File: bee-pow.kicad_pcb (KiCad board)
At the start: 2 copper layers, 29 x 53.3 mm, 34 parts, among them J1 Conn_01x02_Male, J2 Conn_01x02_Male, J3 Conn_01x02_Male, J4 Conn_01x02_Male, J5 Screw_Terminal_01x04, U1 L7805, U2 L7815, U3 L7915

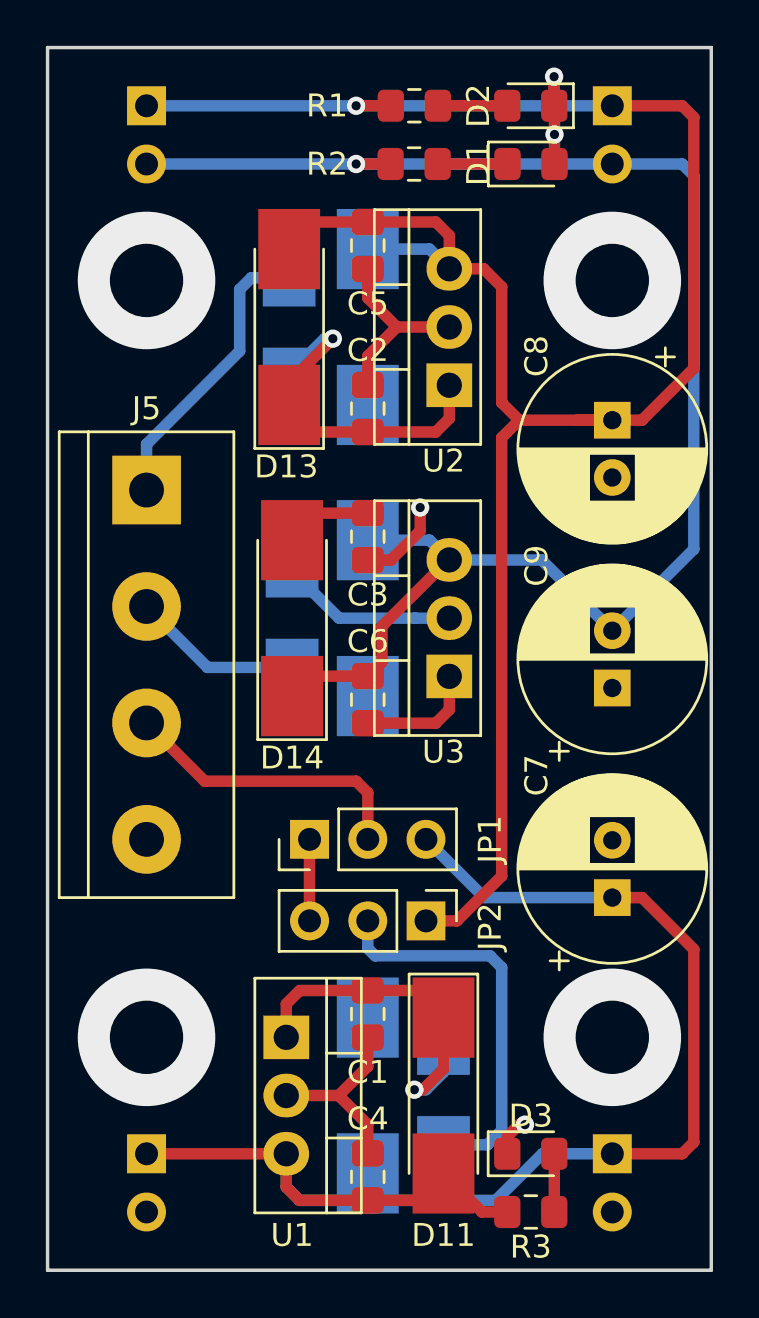
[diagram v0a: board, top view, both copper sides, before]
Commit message: Update labels and mounting holes.
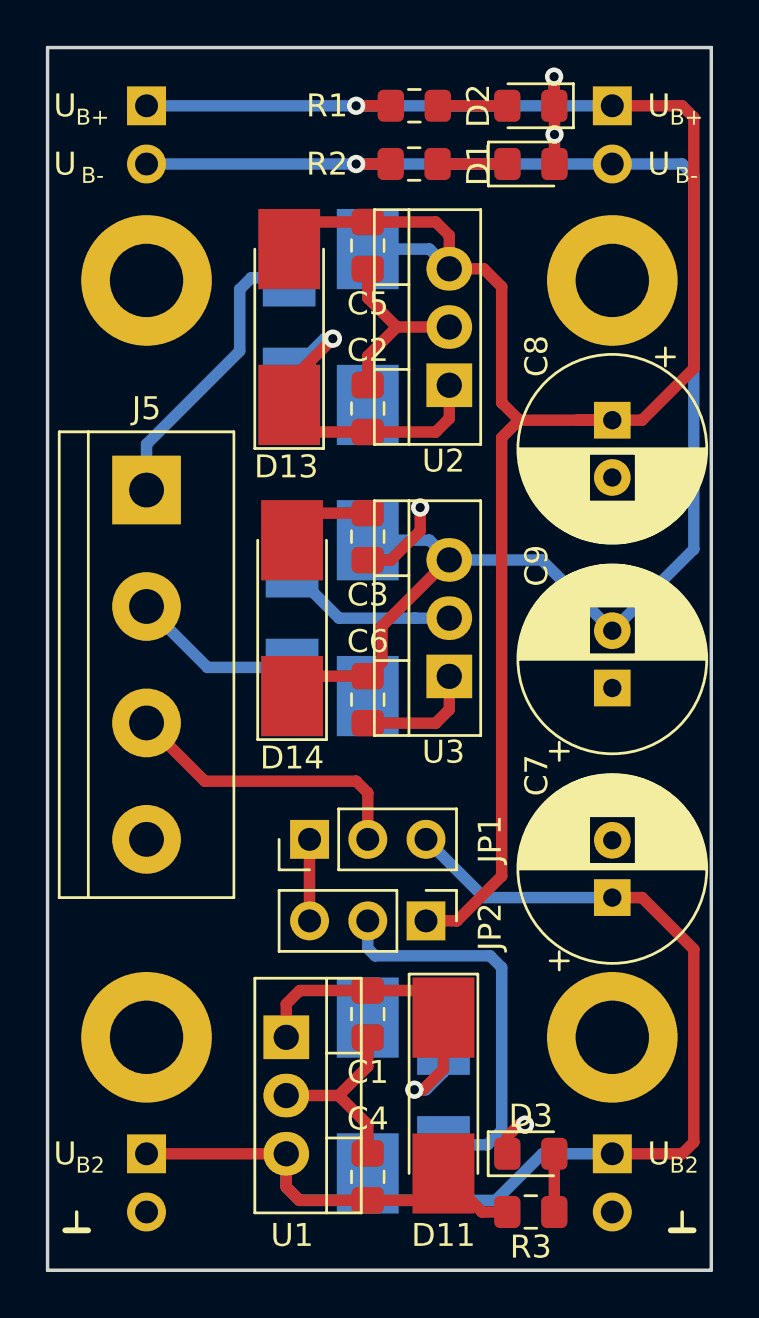
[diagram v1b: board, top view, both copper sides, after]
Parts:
- added H1: Silkscreen_Label, Symbol-emt:Text_U_B+_Silkscreen, F.Cu at (75.2, 91.4)
- added H10: MountingHole_Pad, MountingHole:MountingHole_3.2mm_M3_ISO7380_Pad, F.Cu at (99.1, 99.1)
- added H11: MountingHole_Pad, MountingHole:MountingHole_3.2mm_M3_ISO7380_Pad, F.Cu at (78.7, 132.1)
- added H12: MountingHole_Pad, MountingHole:MountingHole_3.2mm_M3_ISO7380_Pad, F.Cu at (99.1, 132.1)
- added H2: Silkscreen_Label, Symbol-emt:Text_U_B+_Silkscreen, F.Cu at (101.1, 91.4)
- added H3: Silkscreen_Label, Symbol-emt:Text_U_B-_Silkscreen, F.Cu at (75.2, 94.0)
- added H4: Silkscreen_Label, Symbol-emt:Text_U_B-_Silkscreen, F.Cu at (101.1, 94.0)
- added H5: Silkscreen_Label, Symbol-emt:Text_U_B2_Silkscreen, F.Cu at (75.2, 137.2)
- added H6: Silkscreen_Label, Symbol-emt:Text_U_B2_Silkscreen, F.Cu at (101.1, 137.2)
- added H7: Silkscreen_Label, Symbol-emt:Symbol_GND_Silkscreen, F.Cu at (75.7, 139.7)
- added H8: Silkscreen_Label, Symbol-emt:Symbol_GND_Silkscreen, F.Cu at (102.1, 139.7)
- added H9: MountingHole_Pad, MountingHole:MountingHole_3.2mm_M3_ISO7380_Pad, F.Cu at (78.7, 99.1)
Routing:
- net (no net): vias 4 -> 0
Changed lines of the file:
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@@
     (thickness 1.6)
     (drawings 4)
-    (tracks 159)
+    (tracks 155)
     (zones 0)
-    (modules 34)
+    (modules 46)
     (nets 16)
   )
@@
     )
   )
+  (module Symbol-emt:Text_U_B+_Silkscreen (layer F.Cu)
+    (at 75.184 91.44)
+    (descr "Voltage Label Betriebsspannung")
+    (tags "Voltage Label Betriebsspannung")
+    (attr virtual)
+    (fp_text reference H1 (at 0 1.65) (layer F.SilkS) hide
+      (effects (font (size 1 1) (thickness 0.15)))
+    )
+    (fp_text value Silkscreen_Label (at 0 -1.5) (layer F.Fab) hide
+      (effects (font (size 1 1) (thickness 0.15)))
+    )
+    (fp_text user B+ (at 1.2 0.5) (layer F.SilkS)
+      (effects (font (size 0.7 0.7) (thickness 0.1)))
+    )
+    (fp_text user U (at 0 0) (layer F.SilkS)
+      (effects (font (size 1 1) (thickness 0.15)))
+    )
+  )
+  (module Symbol-emt:Text_U_B+_Silkscreen (layer F.Cu)
+    (at 101.092 91.44)
+    (descr "Voltage Label Betriebsspannung")
+    (tags "Voltage Label Betriebsspannung")
+    (attr virtual)
+    (fp_text reference H2 (at 0 1.65) (layer F.SilkS) hide
+      (effects (font (size 1 1) (thickness 0.15)))
+    )
+    (fp_text value Silkscreen_Label (at 0 -1.5) (layer F.Fab) hide
+      (effects (font (size 1 1) (thickness 0.15)))
+    )
+    (fp_text user U (at 0 0) (layer F.SilkS)
+      (effects (font (size 1 1) (thickness 0.15)))
+    )
+    (fp_text user B+ (at 1.2 0.5) (layer F.SilkS)
+      (effects (font (size 0.7 0.7) (thickness 0.1)))
+    )
+  )
+  (module Symbol-emt:Text_U_B-_Silkscreen (layer F.Cu)
+    (at 75.184 93.98)
+    (descr "Voltage Label Betriebsspannung")
+    (tags "Voltage Label Betriebsspannung")
+    (attr virtual)
+    (fp_text reference H3 (at 0 1.65) (layer F.SilkS) hide
+      (effects (font (size 1 1) (thickness 0.15)))
+    )
+    (fp_text value Silkscreen_Label (at 0 -1.5) (layer F.Fab) hide
+      (effects (font (size 1 1) (thickness 0.15)))
+    )
+    (fp_text user B- (at 1.2 0.5) (layer F.SilkS)
+      (effects (font (size 0.7 0.7) (thickness 0.1)))
+    )
+    (fp_text user U (at 0 0) (layer F.SilkS)
+      (effects (font (size 1 1) (thickness 0.15)))
+    )
+  )
+  (module Symbol-emt:Text_U_B-_Silkscreen (layer F.Cu)
+    (at 101.092 93.98)
+    (descr "Voltage Label Betriebsspannung")
+    (tags "Voltage Label Betriebsspannung")
+    (attr virtual)
+    (fp_text reference H4 (at 0 1.65) (layer F.SilkS) hide
+      (effects (font (size 1 1) (thickness 0.15)))
+    )
+    (fp_text value Silkscreen_Label (at 0 -1.5) (layer F.Fab) hide
+      (effects (font (size 1 1) (thickness 0.15)))
+    )
+    (fp_text user U (at 0 0) (layer F.SilkS)
+      (effects (font (size 1 1) (thickness 0.15)))
+    )
+    (fp_text user B- (at 1.2 0.5) (layer F.SilkS)
+      (effects (font (size 0.7 0.7) (thickness 0.1)))
+    )
+  )
+  (module Symbol-emt:Text_U_B2_Silkscreen (layer F.Cu)
+    (at 75.184 137.16)
+    (descr "Voltage Label Betriebsspannung")
+    (tags "Voltage Label Betriebsspannung")
+    (attr virtual)
+    (fp_text reference H5 (at 0 1.65) (layer F.SilkS) hide
+      (effects (font (size 1 1) (thickness 0.15)))
+    )
+    (fp_text value Silkscreen_Label (at 0 -1.5) (layer F.Fab) hide
+      (effects (font (size 1 1) (thickness 0.15)))
+    )
+    (fp_text user B2 (at 1.1 0.5) (layer F.SilkS)
+      (effects (font (size 0.7 0.7) (thickness 0.1)))
+    )
+    (fp_text user U (at 0 0) (layer F.SilkS)
+      (effects (font (size 1 1) (thickness 0.15)))
+    )
+  )
+  (module Symbol-emt:Text_U_B2_Silkscreen (layer F.Cu)
+    (at 101.092 137.16)
+    (descr "Voltage Label Betriebsspannung")
+    (tags "Voltage Label Betriebsspannung")
+    (attr virtual)
+    (fp_text reference H6 (at 0 1.65) (layer F.SilkS) hide
+      (effects (font (size 1 1) (thickness 0.15)))
+    )
+    (fp_text value Silkscreen_Label (at 0 -1.5) (layer F.Fab) hide
+      (effects (font (size 1 1) (thickness 0.15)))
+    )
+    (fp_text user U (at 0 0) (layer F.SilkS)
+      (effects (font (size 1 1) (thickness 0.15)))
+    )
+    (fp_text user B2 (at 1.1 0.5) (layer F.SilkS)
+      (effects (font (size 0.7 0.7) (thickness 0.1)))
+    )
+  )
+  (module Symbol-emt:Symbol_GND_Silkscreen (layer F.Cu)
+    (at 75.692 139.7)
+    (descr "Symbol GND")
+    (tags "Symbol GND")
+    (attr virtual)
+    (fp_text reference H7 (at 0 1.6) (layer F.SilkS) hide
+      (effects (font (size 1 1) (thickness 0.15)))
+    )
+    (fp_text value Silkscreen_Label (at 0 -0.75) (layer F.Fab) hide
+      (effects (font (size 1 1) (thickness 0.15)))
+    )
+    (fp_line (start 0 0.8) (end 0 0) (layer F.SilkS) (width 0.15))
+    (fp_line (start -0.5 0.8) (end 0.5 0.8) (layer F.SilkS) (width 0.25))
+  )
+  (module Symbol-emt:Symbol_GND_Silkscreen (layer F.Cu)
+    (at 102.108 139.7)
+    (descr "Symbol GND")
+    (tags "Symbol GND")
+    (attr virtual)
+    (fp_text reference H8 (at 0 1.6) (layer F.SilkS) hide
+      (effects (font (size 1 1) (thickness 0.15)))
+    )
+    (fp_text value Silkscreen_Label (at 0 -0.75) (layer F.Fab) hide
+      (effects (font (size 1 1) (thickness 0.15)))
+    )
+    (fp_line (start -0.5 0.8) (end 0.5 0.8) (layer F.SilkS) (width 0.25))
+    (fp_line (start 0 0.8) (end 0 0) (layer F.SilkS) (width 0.15))
+  )
+  (module MountingHole:MountingHole_3.2mm_M3_ISO7380_Pad locked (layer F.Cu)
+    (at 78.74 99.06)
+    (descr "Mounting Hole 3.2mm, M3, ISO7380")
+    (tags "mounting hole 3.2mm m3 iso7380")
+    (attr virtual)
+    (fp_text reference H9 (at 0 -3.85) (layer F.SilkS) hide
+      (effects (font (size 1 1) (thickness 0.15)))
+    )
+    (fp_text value MountingHole_Pad (at 0 3.85) (layer F.Fab)
+      (effects (font (size 1 1) (thickness 0.15)))
+    )
+    (fp_text user %R (at 0.3 0) (layer F.Fab)
+      (effects (font (size 1 1) (thickness 0.15)))
+    )
+    (fp_circle (center 0 0) (end 2.85 0) (layer Cmts.User) (width 0.15))
+    (fp_circle (center 0 0) (end 3.1 0) (layer F.CrtYd) (width 0.05))
+    (pad 1 thru_hole circle (at 0 0) (size 5.7 5.7) (drill 3.2) (layers *.Cu *.Mask)
+      (net 1 GND))
+  )
+  (module MountingHole:MountingHole_3.2mm_M3_ISO7380_Pad locked (layer F.Cu)
+    (at 99.06 99.06)
+    (descr "Mounting Hole 3.2mm, M3, ISO7380")
+    (tags "mounting hole 3.2mm m3 iso7380")
+    (attr virtual)
+    (fp_text reference H10 (at 0 -3.85) (layer F.SilkS) hide
+      (effects (font (size 1 1) (thickness 0.15)))
+    )
+    (fp_text value MountingHole_Pad (at 0 3.85) (layer F.Fab)
+      (effects (font (size 1 1) (thickness 0.15)))
+    )
+    (fp_circle (center 0 0) (end 3.1 0) (layer F.CrtYd) (width 0.05))
+    (fp_circle (center 0 0) (end 2.85 0) (layer Cmts.User) (width 0.15))
+    (fp_text user %R (at 0.3 0) (layer F.Fab)
+      (effects (font (size 1 1) (thickness 0.15)))
+    )
+    (pad 1 thru_hole circle (at 0 0) (size 5.7 5.7) (drill 3.2) (layers *.Cu *.Mask)
+      (net 1 GND))
+  )
+  (module MountingHole:MountingHole_3.2mm_M3_ISO7380_Pad locked (layer F.Cu)
+    (at 78.74 132.08)
+    (descr "Mounting Hole 3.2mm, M3, ISO7380")
+    (tags "mounting hole 3.2mm m3 iso7380")
+    (attr virtual)
+    (fp_text reference H11 (at 0 -3.85) (layer F.SilkS) hide
+      (effects (font (size 1 1) (thickness 0.15)))
+    )
+    (fp_text value MountingHole_Pad (at 0 3.85) (layer F.Fab)
+      (effects (font (size 1 1) (thickness 0.15)))
+    )
+    (fp_text user %R (at 0.3 0) (layer F.Fab)
+      (effects (font (size 1 1) (thickness 0.15)))
+    )
+    (fp_circle (center 0 0) (end 2.85 0) (layer Cmts.User) (width 0.15))
+    (fp_circle (center 0 0) (end 3.1 0) (layer F.CrtYd) (width 0.05))
+    (pad 1 thru_hole circle (at 0 0) (size 5.7 5.7) (drill 3.2) (layers *.Cu *.Mask)
+      (net 1 GND))
+  )
+  (module MountingHole:MountingHole_3.2mm_M3_ISO7380_Pad locked (layer F.Cu)
+    (at 99.06 132.08)
+    (descr "Mounting Hole 3.2mm, M3, ISO7380")
+    (tags "mounting hole 3.2mm m3 iso7380")
+    (attr virtual)
+    (fp_text reference H12 (at 0 -3.85) (layer F.SilkS) hide
+      (effects (font (size 1 1) (thickness 0.15)))
+    )
+    (fp_text value MountingHole_Pad (at 0 3.85) (layer F.Fab)
+      (effects (font (size 1 1) (thickness 0.15)))
+    )
+    (fp_circle (center 0 0) (end 3.1 0) (layer F.CrtYd) (width 0.05))
+    (fp_circle (center 0 0) (end 2.85 0) (layer Cmts.User) (width 0.15))
+    (fp_text user %R (at 0.3 0) (layer F.Fab)
+      (effects (font (size 1 1) (thickness 0.15)))
+    )
+    (pad 1 thru_hole circle (at 0 0) (size 5.7 5.7) (drill 3.2) (layers *.Cu *.Mask)
+      (net 1 GND))
+  )
   (gr_line (start 103.378 88.9) (end 103.378 142.24) (layer Edge.Cuts) (width 0.15))
   (gr_line (start 74.422 142.24) (end 103.378 142.24) (layer Edge.Cuts) (width 0.15))
   (gr_line (start 74.422 88.9) (end 103.378 88.9) (layer Edge.Cuts) (width 0.15))
   (gr_line (start 74.422 88.9) (end 74.422 142.24) (layer Edge.Cuts) (width 0.15))
-  (via (at 78.74 99.06) (size 6) (drill 3.2) (layers F.Cu B.Cu) (net 0) (status 40000))
-  (via (at 99.06 99.06) (size 6) (drill 3.2) (layers F.Cu B.Cu) (net 0) (status 40000))
-  (via (at 99.06 132.08) (size 6) (drill 3.2) (layers F.Cu B.Cu) (net 0) (status 40000))
-  (via (at 78.74 132.08) (size 6) (drill 3.2) (layers F.Cu B.Cu) (net 0) (status 40000))
   (segment (start 96.529 93.971) (end 96.538 93.98) (width 0.5) (layer F.Cu) (net 1))
   (segment (start 88.392 98.561) (end 88.392 99.822) (width 0.5) (layer F.Cu) (net 1))

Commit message: Add ground plane.
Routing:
- added copper zone on F.Cu, net GND
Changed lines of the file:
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@@
-(kicad_pcb (version 20171130) (host pcbnew "(5.1.0)-1")
+(kicad_pcb (version 20171130) (host pcbnew 5.0.2+dfsg1-1~bpo9+1)
   (general
     (thickness 1.6)
@@
     (zone_45_only no)
     (trace_min 0.2)
+    (segment_width 0.2)
+    (edge_width 0.15)
     (via_size 0.8)
     (via_drill 0.4)
@@
     (uvia_min_size 0.2)
     (uvia_min_drill 0.1)
-    (edge_width 0.15)
-    (segment_width 0.2)
     (pcb_text_width 0.3)
     (pcb_text_size 1.5 1.5)
@@
     (polygon
       (pts
+        (xy 74.422 88.9) (xy 103.378 88.9) (xy 103.378 142.24) (xy 74.422 142.24)
+      )
+    )
+  )
+  (zone (net 1) (net_name GND) (layer F.Cu) (hatch edge 0.508)
+    (connect_pads (clearance 0.508))
+    (min_thickness 0.254)
+    (fill yes (arc_segments 16) (thermal_gap 0.508) (thermal_bridge_width 0.508))
+    (polygon
+      (pts

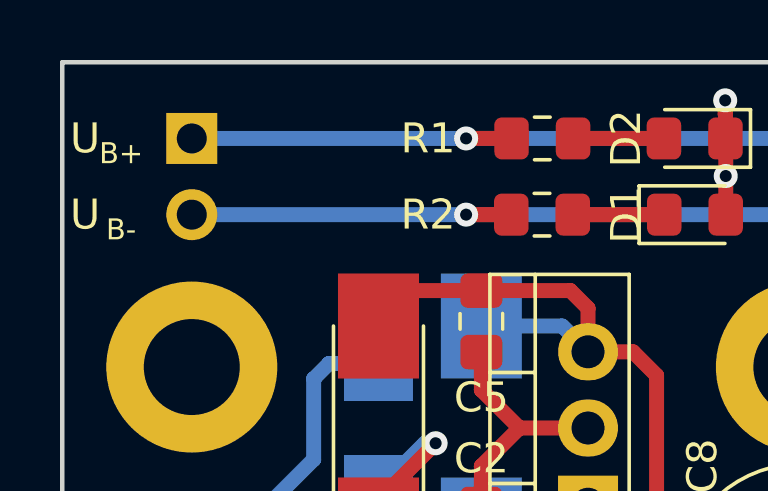
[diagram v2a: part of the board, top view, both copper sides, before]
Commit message: Add text and logos.
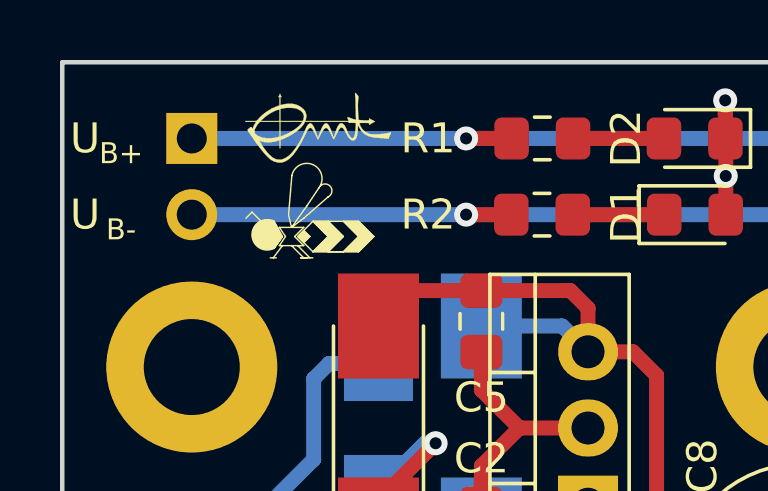
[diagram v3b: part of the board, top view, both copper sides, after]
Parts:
- added H13: Silkscreen_Label, Symbol-emt:EMT-Logo_5.1x2.5mm_Silkscreen, F.Cu at (83.0, 91.1)
- added H14: Silkscreen_Label, Symbol-emt:BEE-Logo_Silkscreen_small, F.Cu at (82.4, 94.7)
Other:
- board text added: "EMT bee-pow rev A"
